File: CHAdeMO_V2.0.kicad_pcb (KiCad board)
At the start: 4 copper layers, 100 x 107.7 mm, 131 parts, among them IC1 ISO1050DUBR, IC2 ISO1050DUBR, J1 UJ2-BV-1-TH, J2 5810132011, J3 39-28-8020, J4 B2B-PH-K-S(LF)(SN), K1 V23086C1001A403-EV-BLBOX, Q1 IRLML0060TRPBF, Q2 IRLML0060TRPBF, Q3 IRLML0060TRPBF, Q4 IRLML0060TRPBF, Q5 DMP4065SQ-7, U1 M24M02-DRMN6TP, U2 ATSAM3X8EA-AU, U3 VOM617A-4T, U4 VOM617A-4T, U5 VOM617A-4T, U6 VOM617A-4T, U7 VOM617A-4T, Y1 CRYSTAL 12MHZ, Y2 Crystal 32.768kHz

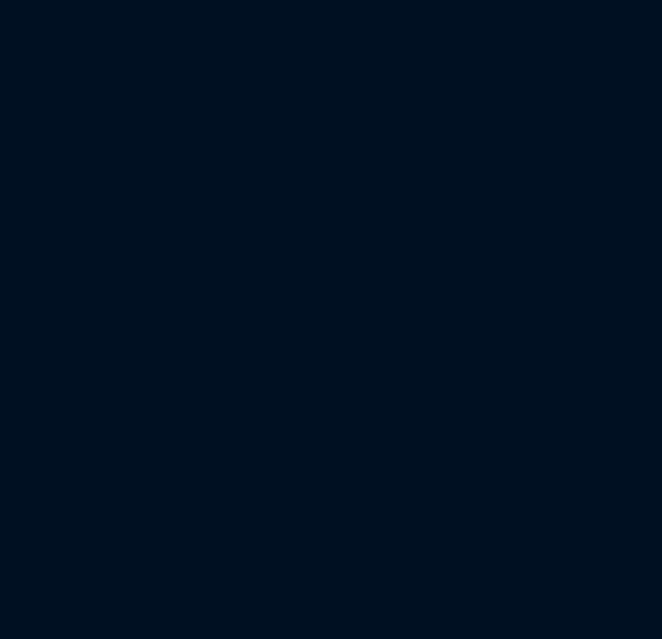
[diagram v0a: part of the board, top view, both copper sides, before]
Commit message: Moved to LQFP100 chip
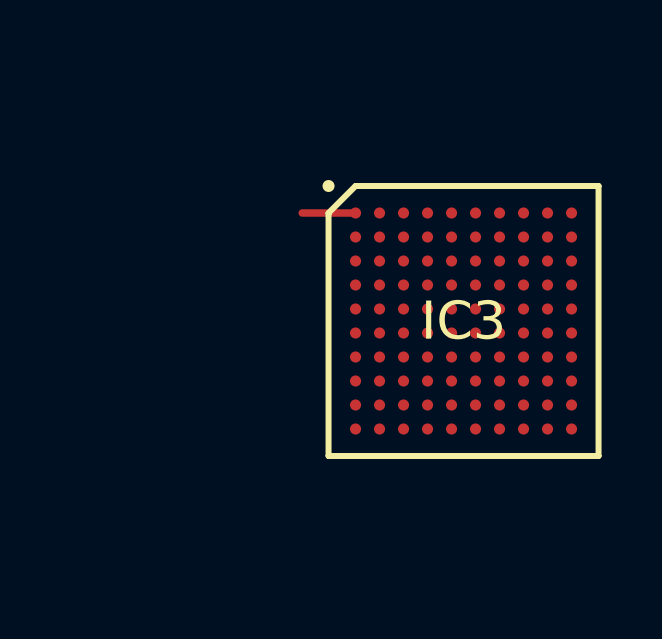
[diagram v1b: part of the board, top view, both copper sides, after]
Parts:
- added IC3: ATSAM3X8CA-CU, SamacSys_Parts:BGA100C80P10X10_900X900X110, F.Cu at (167.6, 126.2)
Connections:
- R2 pad 1: Net-(R2-Pad1) -> Net-(IC3-PadG5)
- U2 pad 24: /CAN0-RX -> Net-(U2-Pad24)
- U2 pad 68: Net-(R2-Pad1) -> Net-(U2-Pad68)
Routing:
- net (no net): track 0.00 -> 7.00 mm
- net +3V3: track 98.9 -> 100.8 mm
- net Net-(IC3-PadA1): track 0.00 -> 1.78 mm

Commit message: V2.0.3 ordered at JLCPCB 23/12
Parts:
- removed C27: 100 nF, Capacitor_SMD:C_1206_3216Metric
- removed S1, S2: PTS647SM38SMTR2LFS, Components:PTS647SK38SMTR2LFS
- removed U2: ATSAM3X8EA-AU, Components:QFP50P2200X2200X145-144N
- moved IC3 73.9 mm to (93.8, 123.4), turned to 180 degrees
- moved R17 69.2 mm to (79.3, 74.1), turned to 270 degrees
- moved R18 25.6 mm to (90.4, 115.5), turned to 0 degrees
- moved C3 16.3 mm to (101.5, 124.9), turned to 0 degrees
- moved Y1 12.7 mm to (101.8, 122.4), turned to 180 degrees
- moved C22 9.75 mm to (92.1, 131.4), turned to 270 degrees
- moved C15 9.20 mm to (98.1, 131.6)
- moved C6 9.20 mm to (95.6, 131.6)
- moved C9 9.20 mm to (100.5, 131.6)
- moved C2 9.05 mm to (102.2, 119.8), turned to 180 degrees
- moved C17 8.75 mm to (102.9, 129.6), turned to 270 degrees
- moved C1 8.15 mm to (89.5, 131.4), turned to 270 degrees
- moved L4 7.15 mm to (104.5, 126.4), turned to 0 degrees
- moved C14 6.25 mm to (105.4, 129.6), turned to 270 degrees
- moved C7 5.45 mm to (87.1, 131.4), turned to 270 degrees
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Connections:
- C3 pad 1: Net-(C3-Pad1) -> /Xout
- IC3 pad A1: Net-(IC3-PadA1) -> /CHAdeMO_contactor2-feedback_D11
- IC3 pad A4: Net-(IC3-PadA4) -> /CAN1-TX
- IC3 pad B9: Net-(IC3-PadB9) -> /CHAdeMO-charge-start1_3.3Vsignal_IN1_D6
- IC3 pad C2: Net-(IC3-PadC2) -> /CHAdeMO-charge-start2_3.3Vsignal_IN2_D7
- IC3 pad C5: Net-(IC3-PadC5) -> /CHAdeMO-charge-enable-signal_D48
- IC3 pad D2: Net-(IC3-PadD2) -> /CAN0-TX
- IC3 pad D4: Net-(IC3-PadD4) -> /VDD_OUT
- IC3 pad D5: Net-(IC3-PadD5) -> +3V3
- IC3 pad D6: Net-(IC3-PadD6) -> /VDD_OUT
- IC3 pad D7: Net-(IC3-PadD7) -> /VDD_OUT
- IC3 pad E2: Net-(IC3-PadE2) -> /relay-CHAdeMO-contactors-signal_D49
- IC3 pad E4: Net-(IC3-PadE4) -> /VDD_OUT
- IC3 pad E5: Net-(IC3-PadE5) -> Earth
- IC3 pad E6: Net-(IC3-PadE6) -> Earth
- IC3 pad E7: Net-(IC3-PadE7) -> +3V3
- IC3 pad F1: Net-(IC3-PadF1) -> /VDD_PLL
- IC3 pad F2: Net-(IC3-PadF2) -> Earth
- IC3 pad F5: Net-(IC3-PadF5) -> Earth
- IC3 pad F6: Net-(IC3-PadF6) -> Earth
- IC3 pad F7: Net-(IC3-PadF7) -> +3V3
- IC3 pad F8: Net-(IC3-PadF8) -> /EEPROM-SCL
- IC3 pad G1: Net-(IC3-PadG1) -> /Xout
- IC3 pad G10: Net-(IC3-PadG10) -> /EEPROM-SDA
- IC3 pad G2: Net-(IC3-PadG2) -> /VDD_OUT_MI
- IC3 pad G4: Net-(IC3-PadG4) -> Earth
- IC3 pad H1: Net-(IC3-PadH1) -> Net-(C2-Pad1)
- IC3 pad H2: Net-(IC3-PadH2) -> Earth
- IC3 pad H4: Net-(IC3-PadH4) -> +3V3
- IC3 pad H7: Net-(IC3-PadH7) -> /CHAdeMO_contactor1-feedback_D27
- IC3 pad J1: Net-(IC3-PadJ1) -> +5V_USB
- IC3 pad J2: Net-(IC3-PadJ2) -> /DHSDP
- IC3 pad J3: Net-(IC3-PadJ3) -> /DHSDM
- IC3 pad J4: Net-(IC3-PadJ4) -> Earth
- IC3 pad J5: Net-(IC3-PadJ5) -> Net-(C4-Pad1)
- IC3 pad J6: Net-(IC3-PadJ6) -> +3V3
- IC3 pad K1: Net-(IC3-PadK1) -> Net-(C13-Pad1)
- IC3 pad K10: Net-(IC3-PadK10) -> /CAN1-RX
- IC3 pad K2: Net-(IC3-PadK2) -> /DFSDP
- IC3 pad K3: Net-(IC3-PadK3) -> /DFSDM
- IC3 pad K4: Net-(IC3-PadK4) -> /VDD_OUT
- IC3 pad K5: Net-(IC3-PadK5) -> Net-(C5-Pad1)
- IC3 pad K6: Net-(IC3-PadK6) -> /VDD_OUT
- IC3 pad K7: Net-(IC3-PadK7) -> /VDD_ANA
- IC3 pad K8: Net-(IC3-PadK8) -> Earth
- IC3 pad K9: Net-(IC3-PadK9) -> Net-(C18-Pad1)
- J1 pad 2: /USB_D- -> /DHSDM
- J1 pad 3: /USB_D+ -> /DHSDP
- J2 pad A4: /USB_D- -> /DHSDM
- J2 pad A5: /USB_D+ -> /DHSDP
- R3 pad 1: Net-(R3-Pad1) -> Net-(IC3-PadH5)
- R6 pad 1: /USB_D- -> /DHSDM
- R6 pad 2: Net-(R6-Pad2) -> /DFSDM
- R7 pad 1: /USB_D+ -> /DHSDP
- R7 pad 2: Net-(R7-Pad2) -> /DFSDP
- Y1 pad 3: Net-(C3-Pad1) -> /Xout
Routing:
- net /DHSDM: track 0.00 -> 99.8 mm, vias 0 -> 1
- net /DHSDP: track 0.00 -> 98.6 mm, vias 0 -> 1
- net /USB_D-: track 77.9 -> 0.00 mm
- net /USB_D+: track 70.9 -> 0.00 mm
- net /MASTER-RESET: track 28.0 -> 0.00 mm
- net Earth: track 189.8 -> 164.5 mm, vias 71 -> 39
- net /CHAdeMO_contactor2-feedback_D11: track 74.7 -> 98.1 mm
- net Net-(IC3-PadH5): track 0.00 -> 20.9 mm, vias 0 -> 2
- net /DFSDM: track 0.00 -> 20.7 mm
- net /DFSDP: track 0.00 -> 19.4 mm
- net Net-(S2-Pad4): track 18.2 -> 0.00 mm
- net /VDD_OUT: track 101.0 -> 83.3 mm, vias 2 -> 7
- net +3V3: track 100.8 -> 84.0 mm
- net Net-(IC3-PadG5): track 0.00 -> 15.9 mm, vias 0 -> 2
- net Net-(R6-Pad2): track 13.5 -> 0.00 mm
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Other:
- rule via_min_drill: 0.3 -> 0.2
- board text added: "CHAdeMO Controller v2.0.3 Lars Rengersen 2021"
- board text removed: "(erase)"
- board text removed: "(reset)"
- board text removed: "CHAdeMO Controller v2.0.1 Lars Rengersen 2020"
